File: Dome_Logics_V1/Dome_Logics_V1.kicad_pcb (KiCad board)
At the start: 4 copper layers, 54.9 x 51.8 mm, 33 parts, among them J1 USB_B_Micro, J12 SERIAL_FU, J2 Rear Logics, J3 Front Logics, J5 12OUT, J7 5V OUT, SW1 SW_Push, U1 ESP32-WROOM-32D_16MB_, U2 CJ2301_S1, U3 ME6211C33M5G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

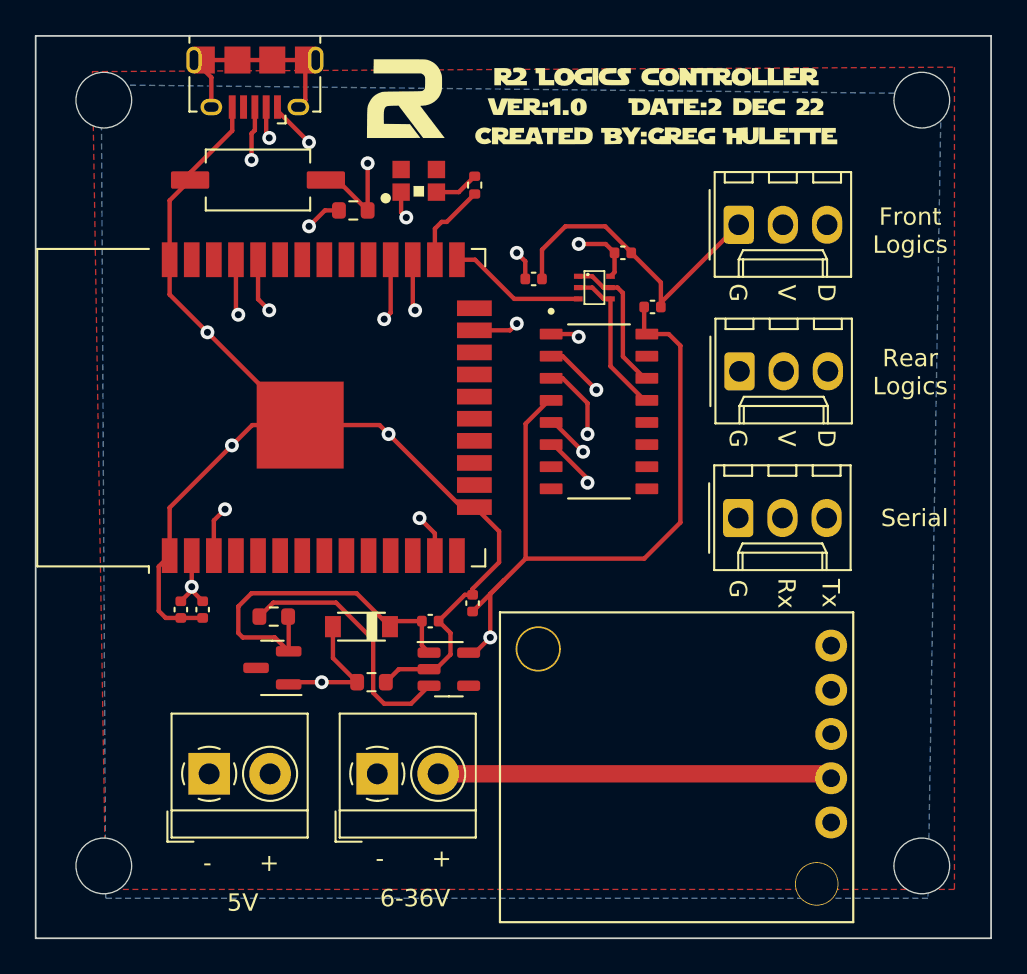
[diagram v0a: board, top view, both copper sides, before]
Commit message: Added a 4th pin to the dome logics controller to support the curved LEDs, in case anyone wants to order them besides myself
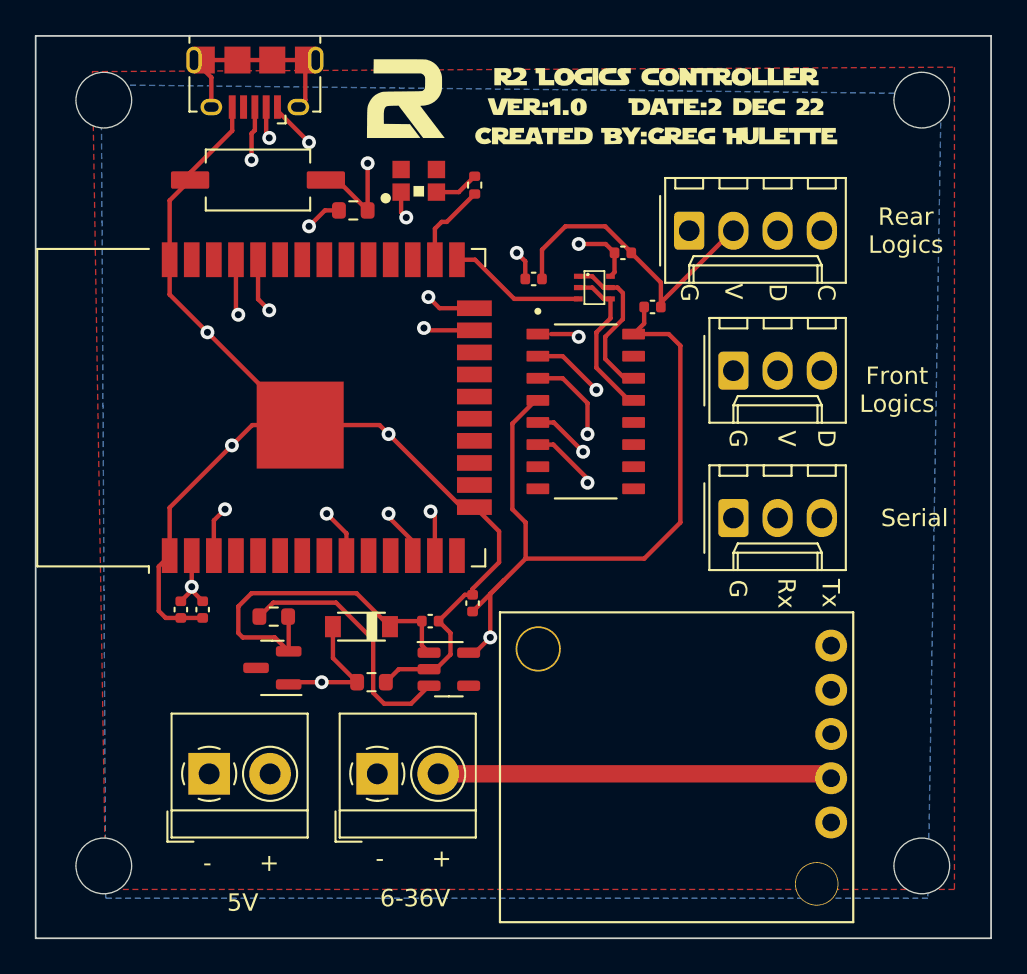
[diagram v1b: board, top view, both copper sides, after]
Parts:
- J2: value Rear Logics -> Conn_01x04; footprint Connector_Molex:Molex_KK-254_AE-6410-03A_1x03_P2.54mm_Vertical -> Connector_Molex:Molex_KK-254_AE-6410-04A_1x04_P2.54mm_Vertical
- moved J2 8.58 mm to (121.6, 92.3)
- moved J3 8.39 mm to (124.2, 100.3)
- moved U4 0.76 mm to (115.7, 102.6)
- moved J12 0.28 mm to (124.2, 108.8)
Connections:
- U1 pad 12: unconnected-(U1-Pad12) -> TX_FU
- U1 pad 23: TX_FU -> FRONT_LOGICS
- U1 pad 24: unconnected-(U1-Pad24) -> REAR_LOGICS_CLOCK
- U1 pad 27: FRONT_LOGICS -> unconnected-(U1-Pad27)
- U1 pad 28: REAR_LOGICS -> unconnected-(U1-Pad28)
- U1 pad 9: unconnected-(U1-Pad9) -> REAR_LOGICS
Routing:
- net REAR_LOGICS_CLOCK: track 0.00 -> 29.7 mm, vias 0 -> 1
- net REAR_LOGICS: track 31.3 -> 57.4 mm
- net TX_FU: track 26.5 -> 31.3 mm
- net FRONT_LOGICS: track 29.0 -> 27.3 mm
- net +3.3V: track 104.2 -> 105.4 mm
- net TXD0: track 38.6 -> 39.3 mm
- net RXD0: track 27.3 -> 28.0 mm
- net D-: track 48.5 -> 49.3 mm
- net D+: track 45.2 -> 45.9 mm
- net RTS: track 8.51 -> 9.26 mm
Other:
- board text added: "C"

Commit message: added LED PCBs
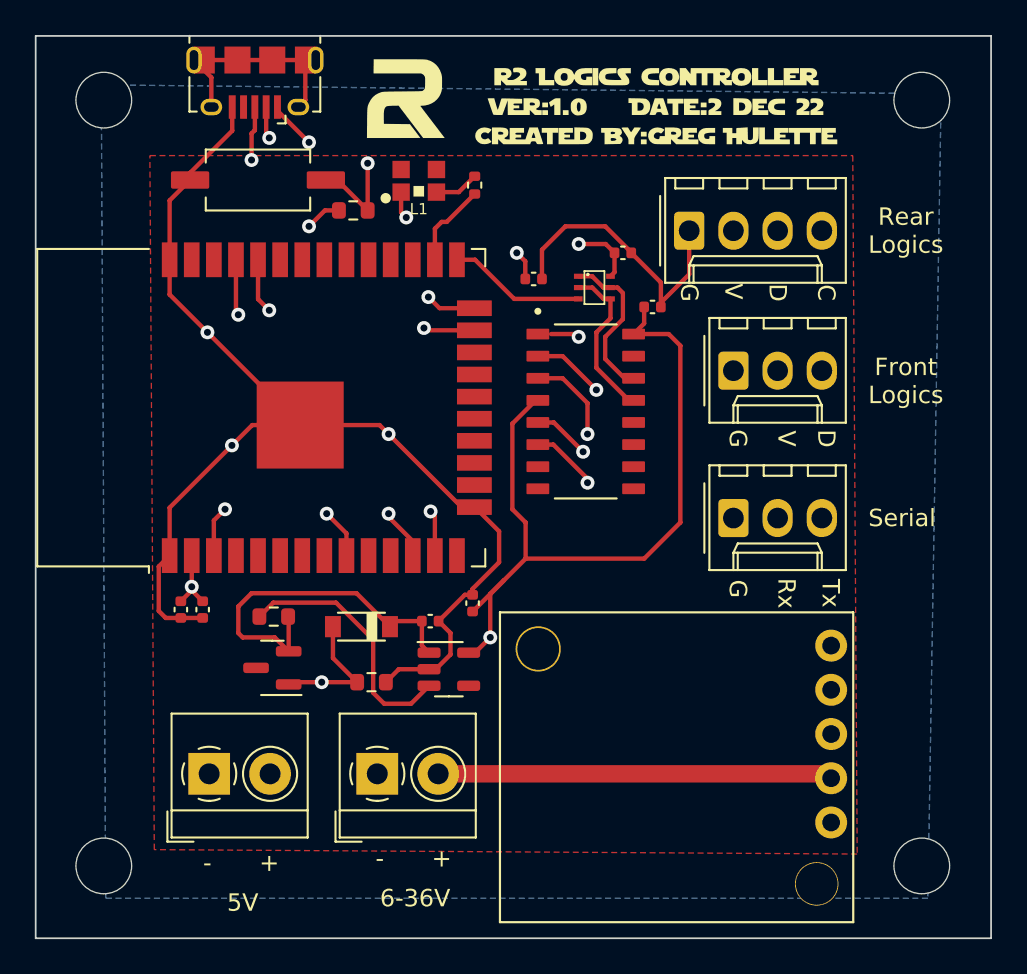
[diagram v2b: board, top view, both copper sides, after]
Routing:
- net GND: track 90.2 -> 88.7 mm
- net REAR_LOGICS_CLOCK: track 29.7 -> 29.2 mm
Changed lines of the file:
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@@
       (drillshape 0)
       (scaleselection 1)
-      (outputdirectory "Gerber/Dome_ControllerV2.0/")
+      (outputdirectory "Gerber/Dome_Logics_Controller_V1.0_5DEC22/")
     )
   )
@@
     (descr "Molex KK-254 Interconnect System, old/engineering part number: AE-6410-04A example for new part number: 22-27-2041, 4 Pins (http://www.molex.com/pdm_docs/sd/022272021_sd.pdf), generated with kicad-footprint-generator")
     (tags "connector Molex KK-254 vertical")
+    (property "LCSC" "C240840")
     (property "Sheetfile" "Dome_Logics_V1.kicad_sch")
     (property "Sheetname" "")
@@
     (fp_line (start -1.27 -0.5) (end -0.562893 0) (layer "F.Fab") (width 0.1))
     (fp_line (start 8.89 2.88) (end 8.89 -2.92) (layer "F.Fab") (width 0.1))
-    (pad "1" thru_hole roundrect locked (at 0 0) (size 1.74 2.19) (drill 1.19) (layers *.Cu *.Mask) (roundrect_rratio 0.143678)
+    (pad "1" thru_hole roundrect locked (at 0 0) (size 1.74 2.19) (drill 1.19) (layers *.Cu *.Mask) (roundrect_rratio 0.1436781609)
       (net 2 "GND") (pinfunction "Pin_1") (pintype "passive"))
     (pad "2" thru_hole oval locked (at 2.54 0) (size 1.74 2.19) (drill 1.19) (layers *.Cu *.Mask)
@@
     (fp_line (start -1.27 2.88) (end 6.35 2.88) (layer "F.Fab") (width 0.1))
     (fp_line (start -1.27 -0.5) (end -0.562893 0) (layer "F.Fab") (width 0.1))
-    (pad "1" thru_hole roundrect locked (at 0 0) (size 1.74 2.19) (drill 1.19) (layers *.Cu *.Mask) (roundrect_rratio 0.143678)
+    (pad "1" thru_hole roundrect locked (at 0 0) (size 1.74 2.19) (drill 1.19) (layers *.Cu *.Mask) (roundrect_rratio 0.1436781609)
       (net 2 "GND") (pinfunction "Pin_1") (pintype "passive"))
     (pad "2" thru_hole oval locked (at 2.54 0) (size 1.74 2.19) (drill 1.19) (layers *.Cu *.Mask)
@@
     (property "Sheetname" "")
     (attr through_hole)
-    (fp_text reference "L1" (at 0 -1.624) (layer "F.SilkS") hide
+    (fp_text reference "L1" (at 0 -1.624 180) (layer "F.SilkS")
       (effects (font (size 0.64 0.64) (thickness 0.15)))
     )
-    (fp_text value "WS2812B-2020" (at 0 0) (layer "F.Fab") hide
+    (fp_text value "WS2812B-2020" (at 0 0 180) (layer "F.Fab")
       (effects (font (size 0.787402 0.787402) (thickness 0.15)))
     )
@@
       (net 6 "unconnected-(L1-Pad1)") (pinfunction "DO") (pintype "bidirectional+no_connect"))
     (pad "2" smd rect (at 1.015 -0.65 180) (size 1 1) (layers "F.Cu" "F.Paste" "F.Mask")
-      (net 2 "GND") (pinfunction "VSS") (pintype "bidirectional"))
+      (net 2 "GND") (pinfunction "GND") (pintype "bidirectional"))
     (pad "3" smd rect (at -1.015 -0.65 180) (size 1 1) (layers "F.Cu" "F.Paste" "F.Mask")
       (net 47 "Net-(L1-Pad3)") (pinfunction "DI") (pintype "bidirectional"))
     (pad "4" smd rect (at -1.015 0.65 180) (size 1 1) (layers "F.Cu" "F.Paste" "F.Mask")
       (net 13 "+5V") (pinfunction "VDD") (pintype "bidirectional"))
-    (model "/Users/gregoryhulette/Downloads/ws2812c-2020-led-1.snapshot.7 (1)/LED_WS2812_2020.step"
-      (offset (xyz 0 0 0))
-      (scale (xyz 1 1 1))
-      (rotate (xyz 0 0 0))
-    )
   )
   (footprint "Package_TO_SOT_SMD:SOT-23" (layer "F.Cu")
@@
     (fp_line (start -1.27 2.88) (end 6.35 2.88) (layer "F.Fab") (width 0.1))
     (fp_line (start -0.562893 0) (end -1.27 0.5) (layer "F.Fab") (width 0.1))
-    (pad "1" thru_hole roundrect locked (at 0 0) (size 1.74 2.19) (drill 1.19) (layers *.Cu *.Mask) (roundrect_rratio 0.143678)
+    (pad "1" thru_hole roundrect locked (at 0 0) (size 1.74 2.19) (drill 1.19) (layers *.Cu *.Mask) (roundrect_rratio 0.1436781609)
       (net 2 "GND") (pinfunction "Pin_1") (pintype "passive"))
     (pad "2" thru_hole oval locked (at 2.54 0) (size 1.74 2.19) (drill 1.19) (layers *.Cu *.Mask)
@@
     (effects (font (size 1 1) (thickness 0.15)) (justify mirror))
   )
-  (gr_text "Serial" (at 134.59 108.776) (layer "F.SilkS")
+  (gr_text "Serial" (at 133.867714 108.776) (layer "F.SilkS")
     (effects (font (size 1 1) (thickness 0.15)))
   )
@@
     (effects (font (size 1 1) (thickness 0.15)))
   )
-  (gr_text "Front\nLogics" (at 133.574 101.41) (layer "F.SilkS")
+  (gr_text "Front\nLogics" (at 134.082 100.902) (layer "F.SilkS")
     (effects (font (size 1 1) (thickness 0.15)))
   )
@@
     (effects (font (size 1 1) (thickness 0.15)))
   )
-  (segment (start 106.777 108.395) (end 106.65 108.268) (width 0.25) (layer "F.Cu") (net 1))
   (segment (start 107.023 110.932) (end 107.023 108.641) (width 0.25) (layer "F.Cu") (net 1))
   (segment (start 107.023 108.641) (end 106.777 108.395) (width 0.25) (layer "F.Cu") (net 1))
@@
   (segment (start 91.56 114.514) (end 91.156 114.11) (width 0.254) (layer "F.Cu") (net 2))
   (segment (start 116.81 92.012) (end 114.524 92.012) (width 0.254) (layer "F.Cu") (net 2))
-  (segment (start 120.008 96.396) (end 120.008 96.646) (width 0.254) (layer "F.Cu") (net 2))
   (segment (start 109.293 108.147) (end 108.561 108.147) (width 0.254) (layer "F.Cu") (net 2))
   (segment (start 99.283 103.432) (end 93.9545 98.1035) (width 0.254) (layer "F.Cu") (net 2))
@@
   (segment (start 114.524 92.012) (end 113.178 93.358) (width 0.254) (layer "F.Cu") (net 2))
   (segment (start 91.783 93.932) (end 91.783 90.527) (width 0.254) (layer "F.Cu") (net 2))
+  (segment (start 120.008 96.396) (end 120.008 96.646) (width 0.254) (layer "F.Cu") (net 2))
   (segment (start 107.92 115.38) (end 107.236 114.696) (width 0.254) (layer "F.Cu") (net 2))
   (segment (start 115.127 98.203) (end 115.286 98.362) (width 0.254) (layer "F.Cu") (net 2))
   (segment (start 105.083 91.207) (end 105.38 91.504) (width 0.254) (layer "F.Cu") (net 2))
+  (segment (start 121.636 94.768) (end 120.008 96.396) (width 0.254) (layer "F.Cu") (net 2))
   (segment (start 95.3615 104.5995) (end 91.783 108.178) (width 0.254) (layer "F.Cu") (net 2))
   (segment (start 120.008 96.646) (end 120.008 95.238) (width 0.254) (layer "F.Cu") (net 2))
-  (segment (start 124.48 91.924) (end 120.008 96.396) (width 0.254) (layer "F.Cu") (net 2))
   (segment (start 92.959 89.351) (end 92.959 88.939) (width 0.254) (layer "F.Cu") (net 2))
   (segment (start 109.19 113.184) (end 108.748 113.184) (width 0.254) (layer "F.Cu") (net 2))
@@
   (segment (start 95.38 86.518) (end 95.38 85.158) (width 0.254) (layer "F.Cu") (net 2))
   (segment (start 118.306 93.536) (end 118.306 93.508) (width 0.254) (layer "F.Cu") (net 2))
+  (segment (start 121.636 92.266) (end 121.636 94.768) (width 0.254) (layer "F.Cu") (net 2))
   (segment (start 110.714 111.316) (end 110.714 109.538) (width 0.254) (layer "F.Cu") (net 2))
   (segment (start 106.6885 117.46) (end 107.074901 117.46) (width 0.254) (layer "F.Cu") (net 2))
@@
   (via (at 106.65 96.076) (size 0.8) (drill 0.4) (layers "F.Cu" "B.Cu") (net 14))
   (segment (start 113 89.726) (end 126.716 89.726) (width 0.25) (layer "In2.Cu") (net 14))
-  (segment (start 129.56 91.924) (end 129.56 92.47) (width 0.254) (layer "In2.Cu") (net 14))
   (segment (start 126.716 89.726) (end 129.256 92.266) (width 0.25) (layer "In2.Cu") (net 14))
   (segment (start 106.65 96.076) (end 113 89.726) (width 0.25) (layer "In2.Cu") (net 14))
@@
     (polygon
       (pts
-        (xy 136.876 130.112)
-        (xy 88.108 130.112)
-        (xy 87.346 83.122)
-        (xy 136.876 82.868)
+        (xy 131.288 128.08)
+        (xy 90.902 127.826)
+        (xy 90.648 87.948)
+        (xy 131.034 87.948)
       )
     )
